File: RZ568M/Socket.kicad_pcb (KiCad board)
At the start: 2 copper layers, 430 x 65 mm, 13 parts, among them J1 CONNECTOR, J2 CONNECTOR, J3 CONNECTOR, J4 CONNECTOR, J5 CONNECTOR, J6 CONNECTOR, T1 TUBE, T2 TUBE, T3 TUBE, T4 TUBE, T5 TUBE, T6 TUBE

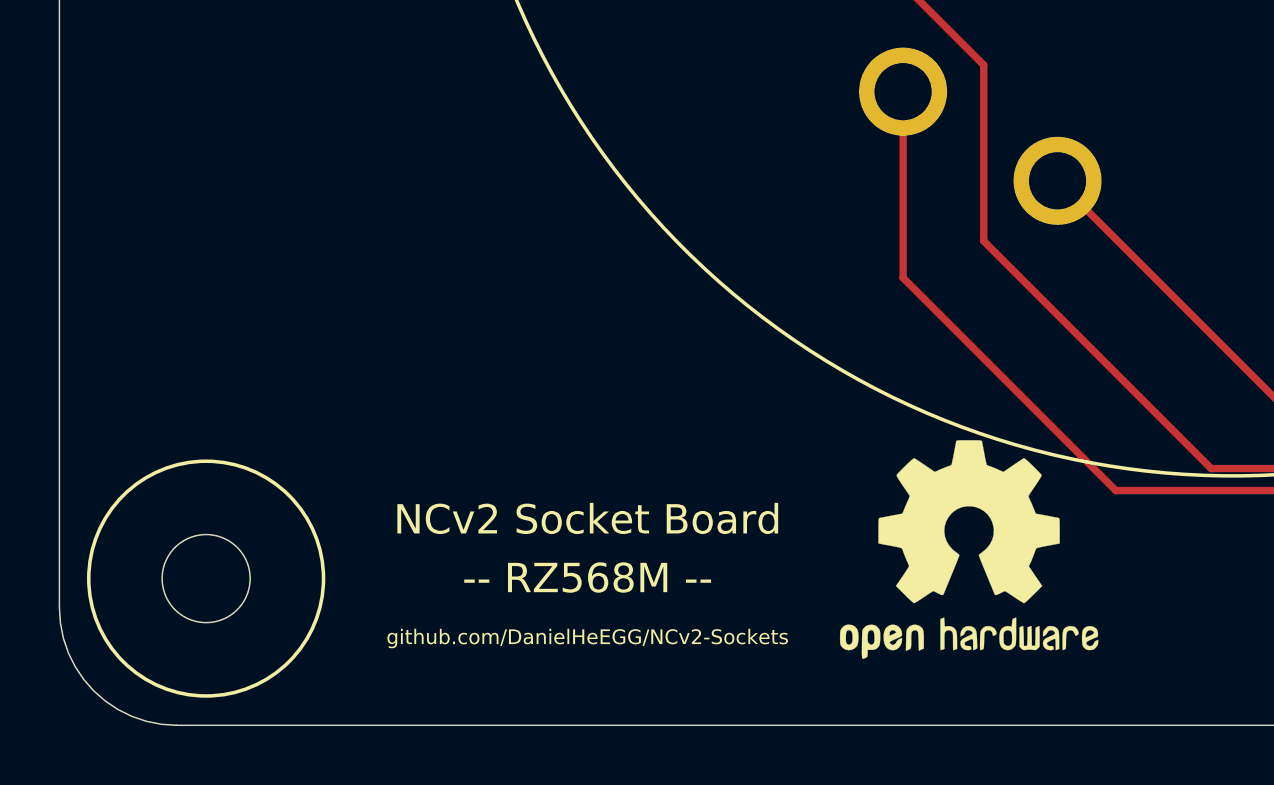
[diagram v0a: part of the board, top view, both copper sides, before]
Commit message: Increase silkscreen text size
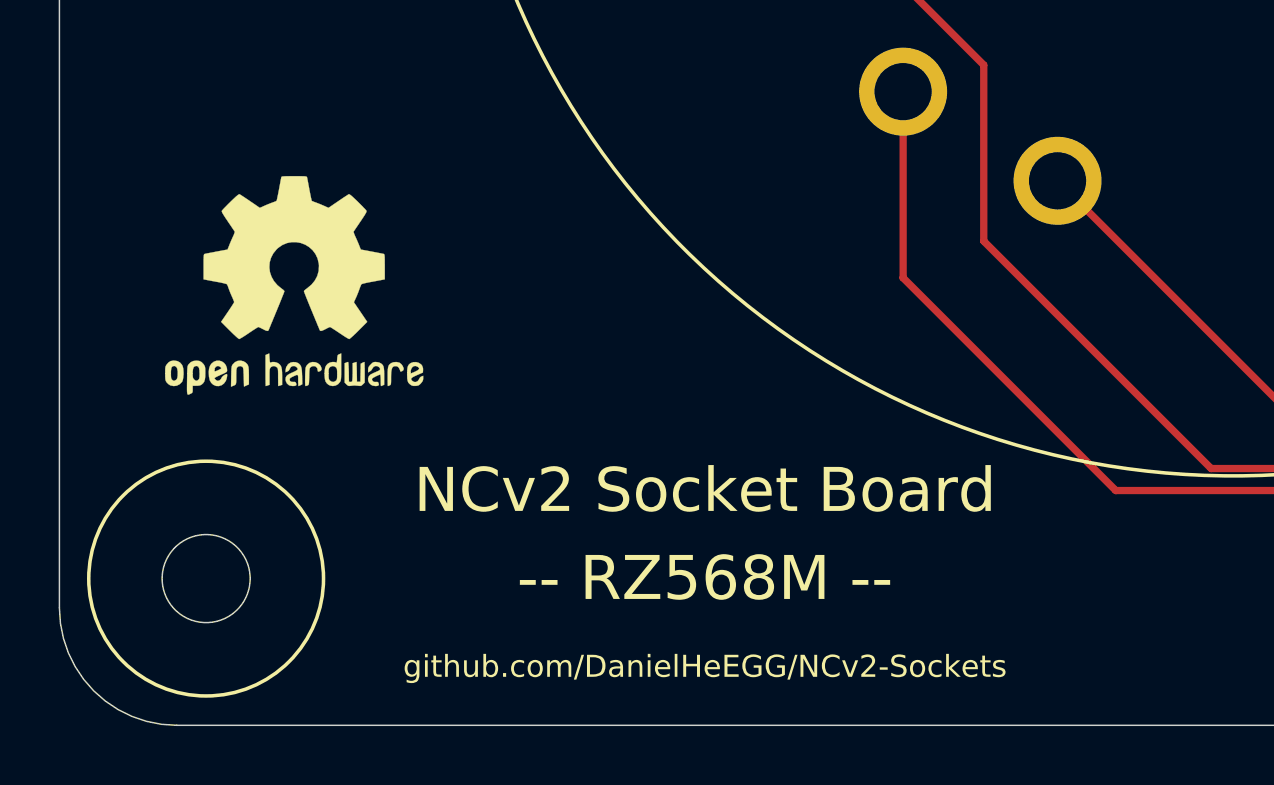
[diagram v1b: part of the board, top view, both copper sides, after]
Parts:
- moved REF** 24.7 mm to (-87.0, 110.0)
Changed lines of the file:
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@@
   )
   (module Symbol:OSHW-Logo2_9.8x8mm_SilkScreen (layer F.Cu)
-    (at -64 119)
+    (at -87 110)
     (descr "Open Source Hardware Symbol")
     (tags "Logo Symbol OSHW")
@@
   (gr_circle (center -20 65) (end -16 65) (layer F.SilkS) (width 0.12))
   (gr_circle (center -20 120) (end -16 120) (layer F.SilkS) (width 0.12))
-  (gr_text "-- RZ568M --" (at -77 120) (layer F.SilkS)
-    (effects (font (size 1 1) (thickness 0.15)))
-  )
-  (gr_text github.com/DanielHeEGG/NCv2-Sockets (at -77 122) (layer F.SilkS)
-    (effects (font (size 0.5 0.5) (thickness 0.1)))
-  )
-  (gr_text "NCv2 Socket Board" (at -77 118) (layer F.SilkS)
-    (effects (font (size 1 1) (thickness 0.15)))
+  (gr_text "-- RZ568M --" (at -73 120) (layer F.SilkS)
+    (effects (font (size 1.5 1.5) (thickness 0.2)))
+  )
+  (gr_text github.com/DanielHeEGG/NCv2-Sockets (at -73 123) (layer F.SilkS)
+    (effects (font (size 0.75 0.75) (thickness 0.1)))
+  )
+  (gr_text "NCv2 Socket Board" (at -73 117) (layer F.SilkS)
+    (effects (font (size 1.5 1.5) (thickness 0.2)))
   )
   (gr_line (start 331 60) (end -91 60) (layer Edge.Cuts) (width 0.05))
@@
   (gr_circle (center 330 120) (end 334 120) (layer F.SilkS) (width 0.12))
   (gr_circle (center 330 120) (end 331.5 120) (layer Edge.Cuts) (width 0.05))
-  (segment (start 24 81.25) (end 30.155444 81.25) (width 0.25) (layer B.Cu) (net 53))
-  (segment (start -0.5 76) (end -0.5 72) (width 0.25) (layer B.Cu) (net 53))
-  (segment (start 1.75 69.75) (end 12.5 69.75) (width 0.25) (layer B.Cu) (net 53))
-  (segment (start 2.5 79) (end -0.5 76) (width 0.25) (layer B.Cu) (net 53))
-  (segment (start 12.5 69.75) (end 24 81.25) (width 0.25) (layer B.Cu) (net 53))
-  (segment (start -0.5 72) (end 1.75 69.75) (width 0.25) (layer B.Cu) (net 53))
   (segment (start 252 120) (end 252 90.75) (width 0.25) (layer F.Cu) (net 1))
   (segment (start 252 90.75) (end 254.75 88) (width 0.25) (layer F.Cu) (net 1))
@@
   (segment (start 11.594223 76.594223) (end 3.751217 76.594223) (width 0.25) (layer B.Cu) (net 52))
   (segment (start 45.25 110.25) (end 11.594223 76.594223) (width 0.25) (layer B.Cu) (net 52))
+  (segment (start 24 81.25) (end 30.155444 81.25) (width 0.25) (layer B.Cu) (net 53))
+  (segment (start -0.5 76) (end -0.5 72) (width 0.25) (layer B.Cu) (net 53))
+  (segment (start 1.75 69.75) (end 12.5 69.75) (width 0.25) (layer B.Cu) (net 53))
+  (segment (start 2.5 79) (end -0.5 76) (width 0.25) (layer B.Cu) (net 53))
+  (segment (start 12.5 69.75) (end 24 81.25) (width 0.25) (layer B.Cu) (net 53))
+  (segment (start -0.5 72) (end 1.75 69.75) (width 0.25) (layer B.Cu) (net 53))
   (segment (start 91.68 120) (end 82.68 111) (width 0.25) (layer B.Cu) (net 53))
   (segment (start 82.68 111) (end 45 111) (width 0.25) (layer B.Cu) (net 53))

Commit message: Migrate to KiCAD 6
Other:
- net class Default removed
